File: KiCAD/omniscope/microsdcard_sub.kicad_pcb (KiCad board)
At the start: 2 copper layers, 41.5 x 21.1 mm, 1 part

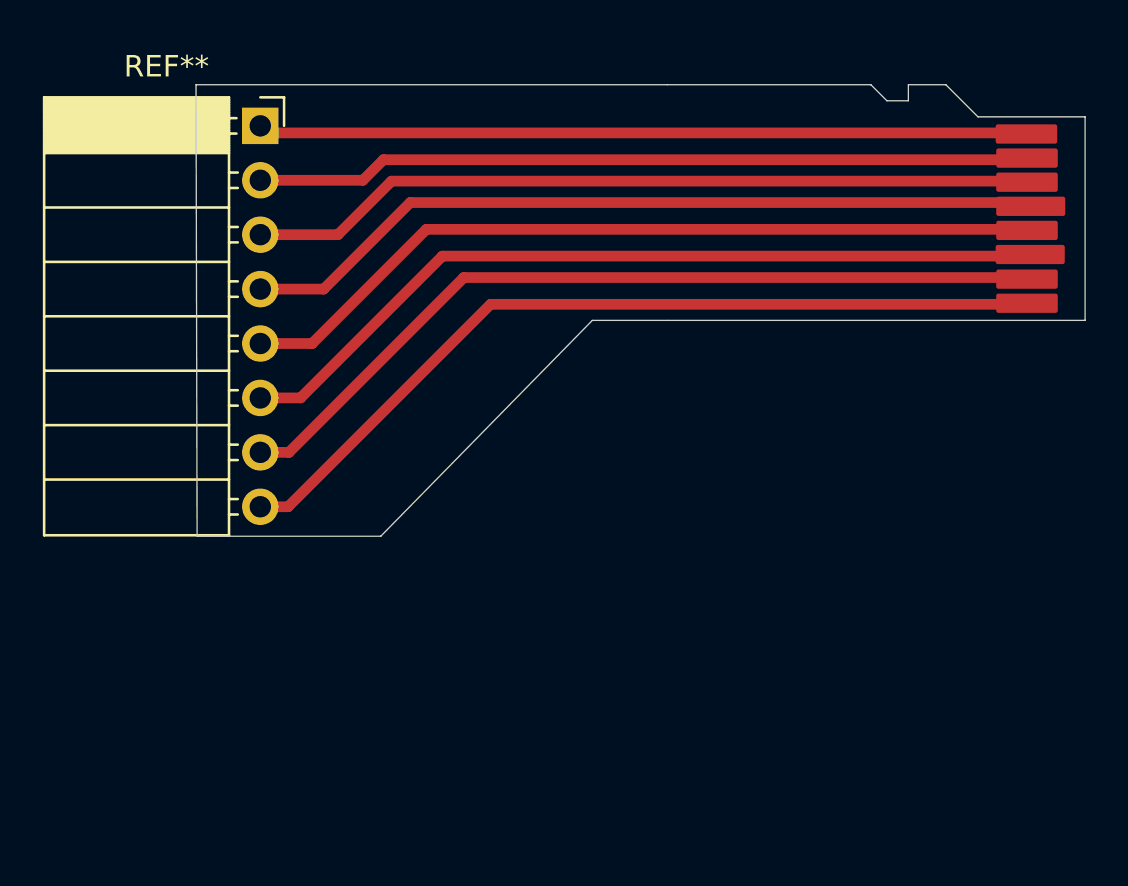
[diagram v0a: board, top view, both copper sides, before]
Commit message: Adding PCB for SD Card
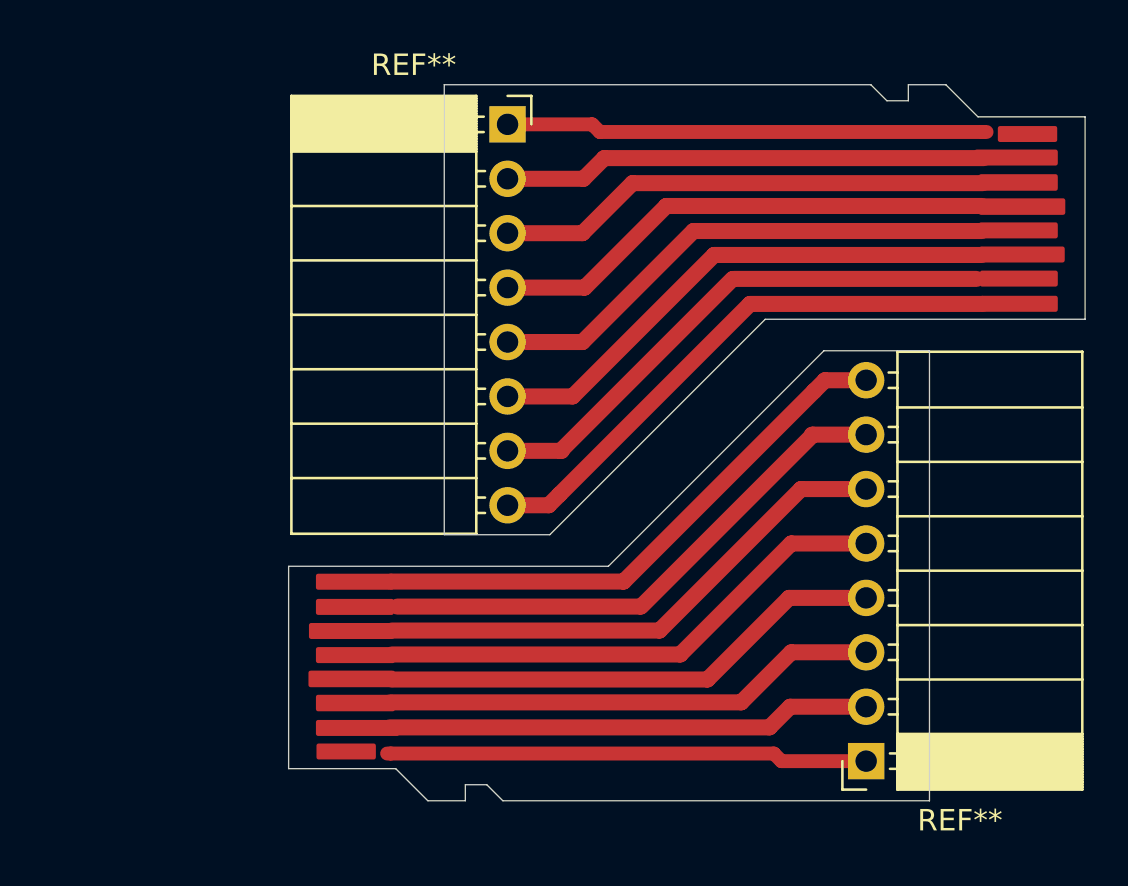
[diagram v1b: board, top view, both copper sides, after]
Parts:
- added REF**: PinSocket_1x08_P2.54mm_Horizontal, Connector_PinSocket_2.54mm:PinSocket_1x08_P2.54mm_Horizontal, F.Cu at (95.0, 90.1)
- moved REF** 11.5 mm to (78.3, 60.4)
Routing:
- net (no net): track 299.2 -> 386.5 mm
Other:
- board size 41.5 x 21.1 mm -> 37.2 x 33.4 mm
